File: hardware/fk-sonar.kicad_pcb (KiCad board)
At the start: 2 copper layers, 34.5 x 70.4 mm, 81 parts, among them J1 Conn_01x03, J2 CONN-HDR-2x5, J3 RF-SMA-EDGE, J4 MICRO-USB, J5 S2B-PH-SM4-TB, J6 Conn_01x04, J7 S2B-PH-SM4-TB, J8 Conn_01x03, J9 Conn_01x05, M1 MOUNT_HOLE, M3 MOUNT_HOLE, M4 MOUNT_HOLE, M6 MOUNT_HOLE, Q1 2N7002LT1G, Q2 2N7002LT1G, Q3 2N7002LT1G, Q4 2N7002LT1G, SW1 SPNO, U1 ATSAMD21G18A-AU, U2 RFM95W, U3 BQ24074RGTT, U4 S25FL116K0XMFI041, U5 MAX1704XX, U6 MCP1700T-3302E/MB, Y1 FC-135

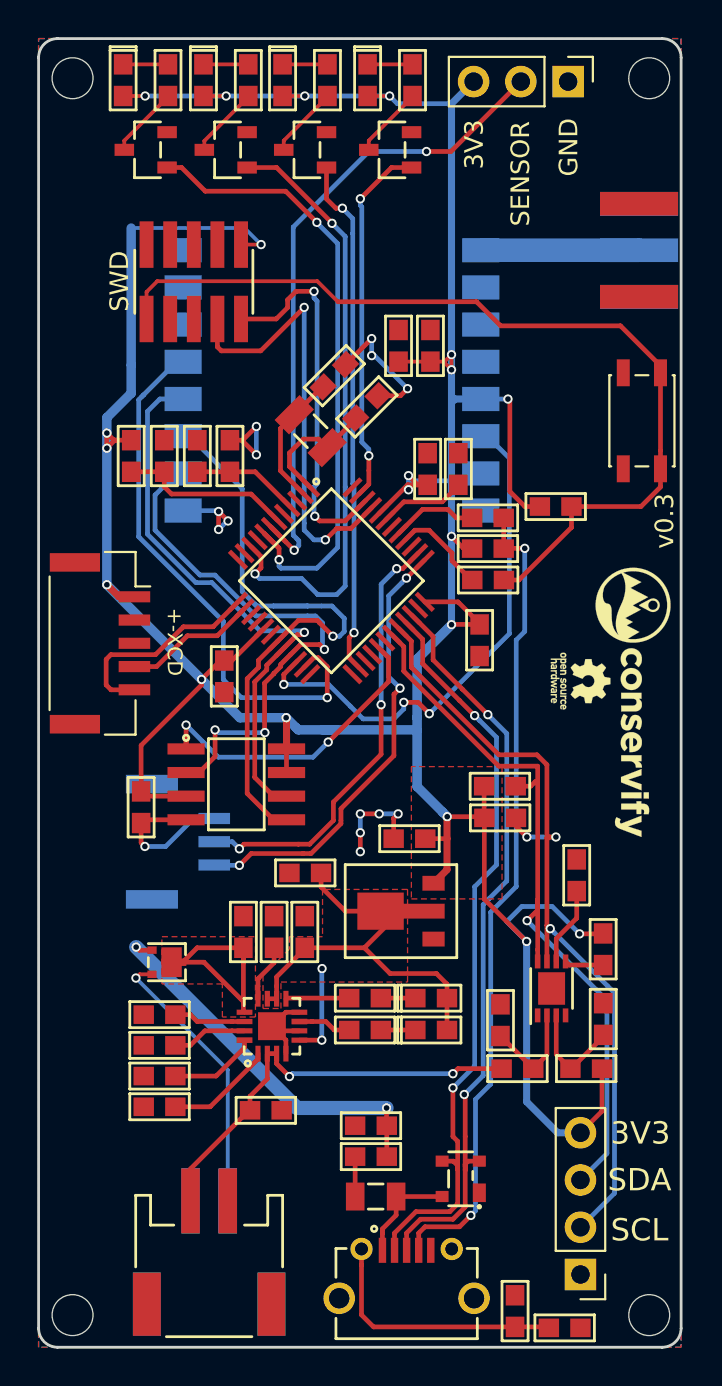
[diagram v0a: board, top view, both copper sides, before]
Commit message: Upgrade to Kicad 5. Also adding SK6812 and molex connectors.
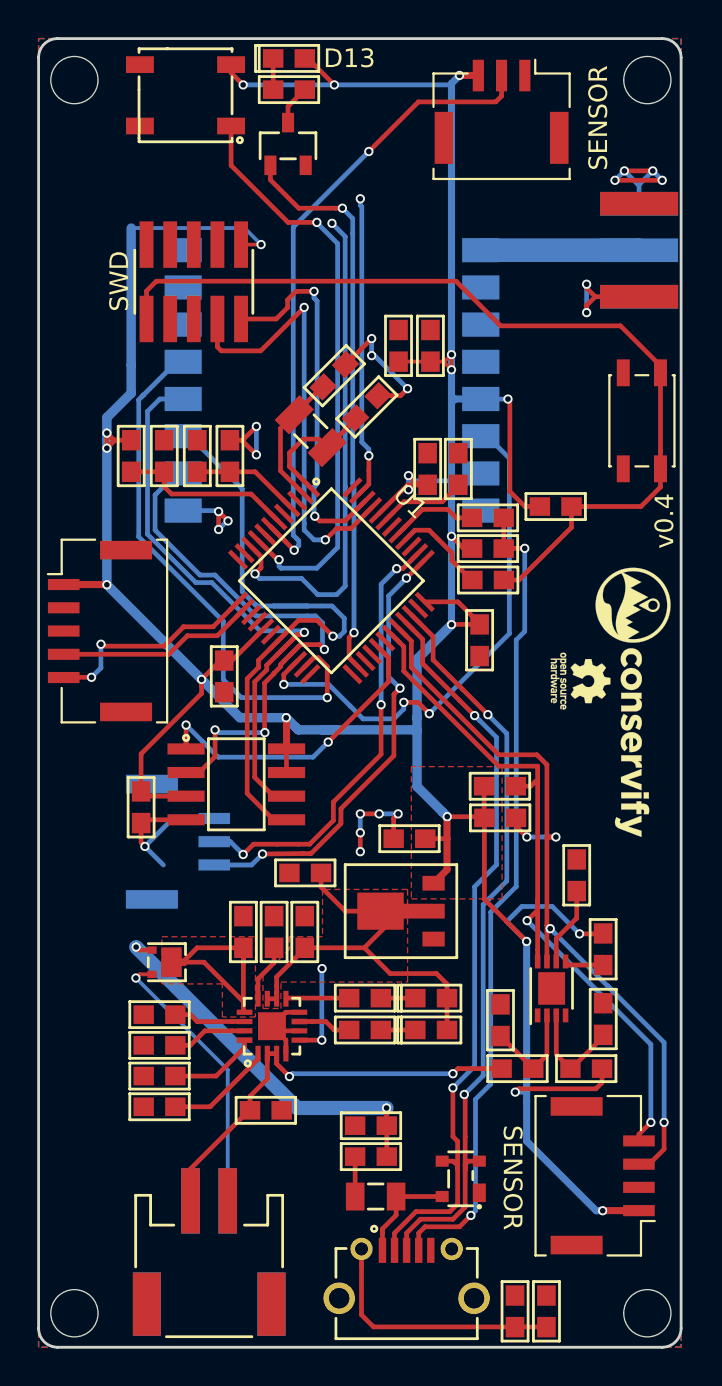
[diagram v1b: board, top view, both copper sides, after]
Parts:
- removed D2: Orange, RocketScreamKicadLibrary:LED-0603
- removed D3: Yellow, RocketScreamKicadLibrary:LED-0603
- removed D4: Blue, RocketScreamKicadLibrary:LED-0603
- removed Q2, Q3, Q4: 2N7002LT1G, RocketScreamKicadLibrary:SOT-23
- removed R4, R5, R6: 2K2, RocketScreamKicadLibrary:RES-0603
- added U7: SK6812, conservify:SK6812, F.Cu at (130.1, 65.3)
- C1, C10, C11, C12, C13, C14, C15, C16, C17, C18, C19, C2, C20, C21, C3, C4, C5, C6, C7, C8, C9: footprint RocketScreamKicadLibrary:CAP-0603 -> conservify:CAP-0603
- D1, D7, D8: footprint RocketScreamKicadLibrary:LED-0603 -> conservify:LED-0603
- D5: footprint RocketScreamKicadLibrary:SOT-1016 -> conservify:SOT-1016
- D6: footprint RocketScreamKicadLibrary:SOT-143B -> conservify:SOT-143B
- F1: footprint RocketScreamKicadLibrary:MF-PSMF020X -> conservify:MF-PSMF020X
- J1: footprint Socket_Strips:Socket_Strip_Straight_1x03_Pitch2.54mm -> conservify:Molex_CLIK-Mate_502382-0370_1x03_P1.25mm_Vertical
- J2: value CONN-HDR-2x5 -> CONN_02x05_SWD; footprint conservify:HDR_2x5_Pitch1.27mm_SMD_JTAG_SWD -> conservify:HDR_02x05_Pitch1.27mm_SMD_SWD
- J3: footprint RocketScreamKicadLibrary:RF-SMA-EDGE -> conservify:RF-SMA-EDGE
- J5, J7: footprint RocketScreamKicadLibrary:S2B-PH-SM4-TB -> conservify:S2B-PH-SM4-TB
- J6: footprint Socket_Strips:Socket_Strip_Straight_1x04_Pitch2.54mm -> conservify:Molex_CLIK-Mate_502382-0470_1x04_P1.25mm_Vertical
- J8: value Conn_01x03 -> CONN_01x03_SERIAL
- J9: footprint conservify:Molex_CLIK-Mate_502386-0570_1x05_P1.25mm_Horizontal -> conservify:Molex_CLIK-Mate_502382-0570_1x05_P1.25mm_Vertical
- L1, L2: footprint RocketScreamKicadLibrary:IND-0603 -> conservify:IND-0603
- M1, M3, M4, M6: footprint RocketScreamKicadLibrary:HOLE_NPTH_2.2MM -> conservify:HOLE_NPTH_2.54MM
- Q1: footprint RocketScreamKicadLibrary:SOT-23 -> conservify:SOT-23
- R1, R10, R11, R12, R13, R14, R15, R16, R17, R18, R19, R2, R20, R21, R22, R3, R7, R8, R9: footprint RocketScreamKicadLibrary:RES-0603 -> conservify:RES-0603
- U1: footprint RocketScreamKicadLibrary:TQFP-48_7x7mm_Pitch0.5mm -> conservify:TQFP-48_7x7mm_Pitch0.5mm
- U2: footprint RocketScreamKicadLibrary:RFM9xW -> conservify:RFM9xW
- U3: footprint RocketScreamKicadLibrary:QFN-16_3x3mm -> conservify:QFN-16_3x3mm
- U4: footprint RocketScreamKicadLibrary:SOIC-8-N -> conservify:SOIC-8-N
- U5: footprint Housings_DFN_QFN:DFN-8-1EP_3x2mm_Pitch0.5mm -> conservify:DFN-8-1EP_3x2mm_Pitch0.5mm
- U6: footprint RocketScreamKicadLibrary:SOT-89 -> conservify:SOT-89
- Y1: footprint RocketScreamKicadLibrary:ABS07 -> conservify:ABS07
- moved D1 8.99 mm to (135.6, 63.3), turned to 0 degrees
- moved Q1 7.66 mm to (135.6, 67.9), turned to 0 degrees
- moved R1 6.52 mm to (135.6, 65.0), turned to 0 degrees
- moved J6 5.44 mm to (152.5, 123.4), turned to 90 degrees
- moved J1 3.93 mm to (147.1, 66.2), turned to 180 degrees
- moved R13 1.32 mm to (149.5, 130.7), turned to 90 degrees
- moved J9 0.66 mm to (125.5, 94.1)
- moved M3 0.14 mm to (124.1, 130.8)
- moved M4 0.14 mm to (154.9, 130.8)
- moved M1 0.14 mm to (154.9, 64.5)
- moved M6 0.14 mm to (124.1, 64.5)
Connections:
- C7 pad 2: GND -> Net-(C7-Pad2)
- J6 pad 1: GND -> 3V3
- J6 pad 2: /SCL1 -> GND
- J6 pad 3: /SDA1 -> /SCL1
- J6 pad 4: 3V3 -> /SDA1
- Q1 pad 1: /A2 -> /D13
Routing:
- net /A2: track 34.7 -> 0.75 mm, vias 2 -> 0
- net /A3: track 0.00 -> 31.5 mm, vias 0 -> 2
- net GND: track 33.3 -> 49.7 mm, vias 14 -> 20
- net /A4: track 32.9 -> 27.1 mm
- net 3V3: track 204.7 -> 209.0 mm, vias 20 -> 21
- net Net-(Q2-Pad3): track 3.88 -> 0.00 mm
- net Net-(Q4-Pad3): track 3.87 -> 0.00 mm
- net Net-(Q3-Pad3): track 3.87 -> 0.00 mm
- net /A5: track 19.7 -> 16.3 mm
- net /SCL3: track 7.77 -> 10.7 mm
- net /D13: track 28.1 -> 30.6 mm
- net Net-(D4-Pad1): track 2.41 -> 0.00 mm
- net Net-(D3-Pad1): track 2.41 -> 0.00 mm
- net Net-(D2-Pad1): track 2.41 -> 0.00 mm
- net Net-(Q1-Pad3): track 3.87 -> 2.14 mm
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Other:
- board text added: "D13"
- board text added: "v0.4"
- board text removed: "+-XCD"
- board text removed: "3V3"
- board text removed: "GND"
- board text removed: "SCL"
- board text removed: "SDA"
- board text removed: "v0.3"

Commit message: Silkscreen cleanup.
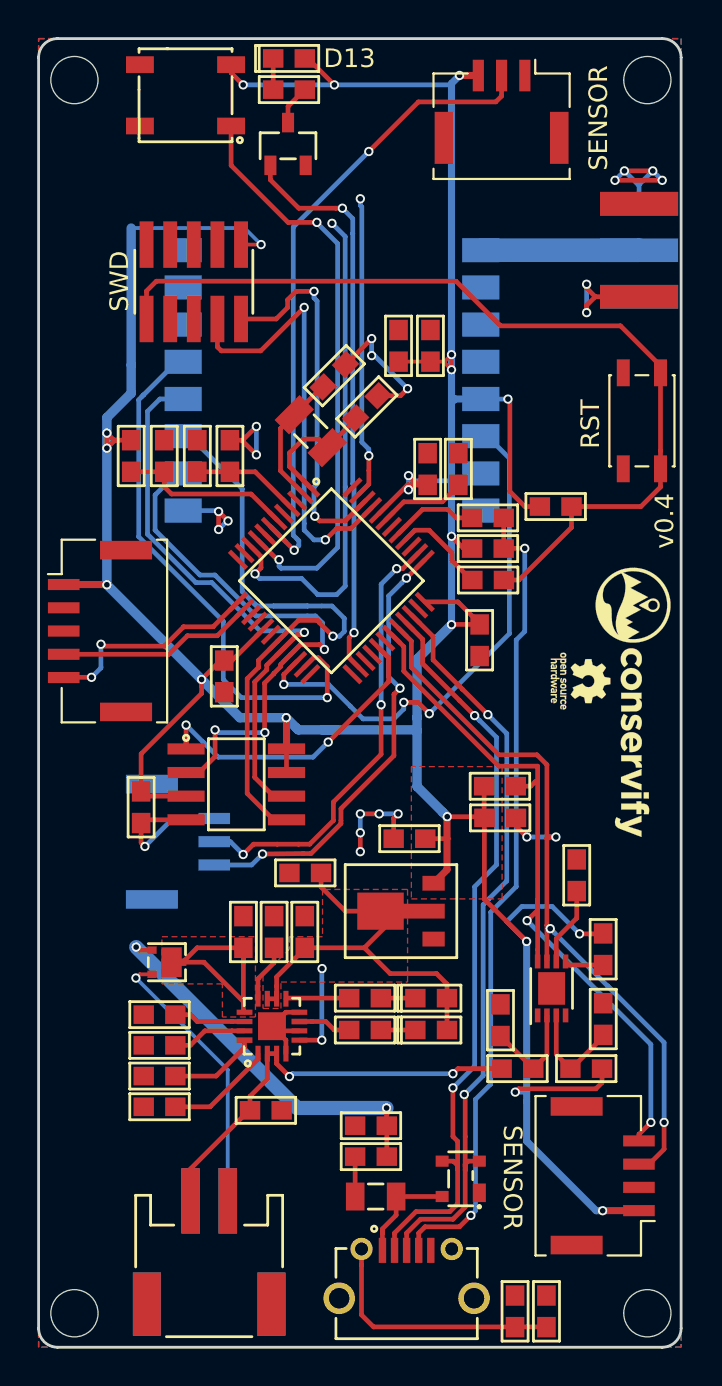
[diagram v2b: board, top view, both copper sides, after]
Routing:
- net GND: track 49.7 -> 48.3 mm
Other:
- board text added: "RST"

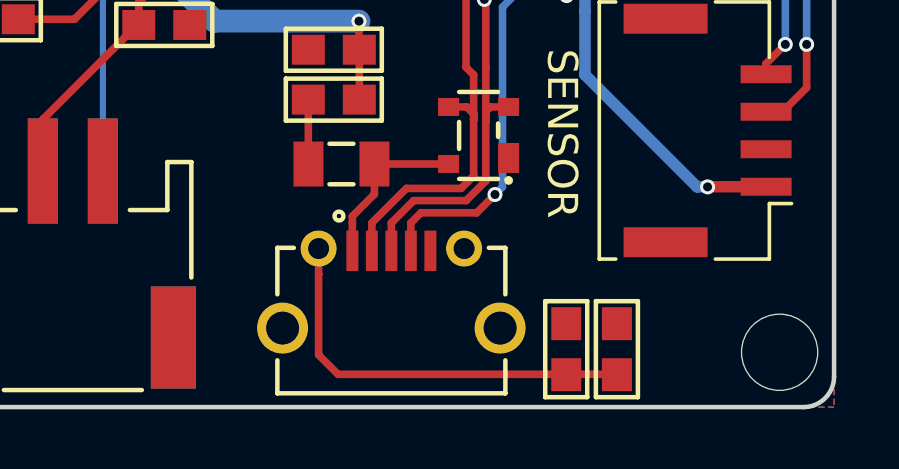
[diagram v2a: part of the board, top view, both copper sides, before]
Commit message: New USB for vertical entry.
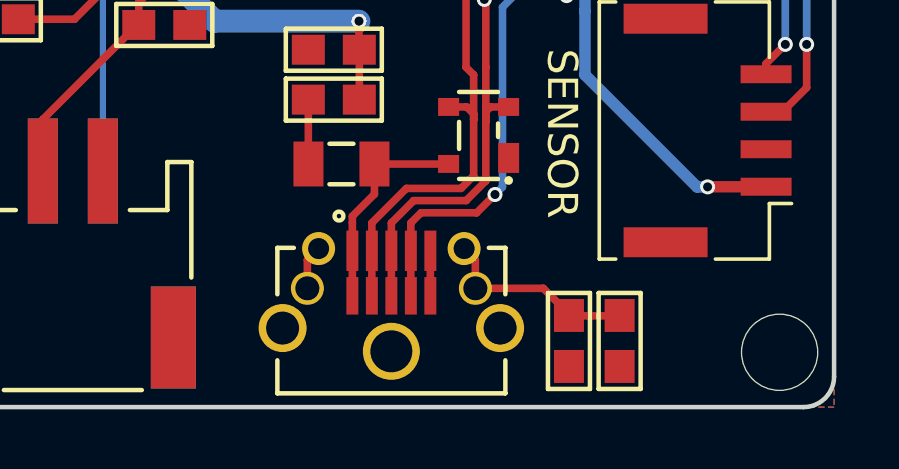
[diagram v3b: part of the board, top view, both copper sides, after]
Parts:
- moved C14 1.80 mm to (149.6, 130.4), turned to 270 degrees
- moved R13 1.62 mm to (147.9, 130.4), turned to 270 degrees
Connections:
- J4 pad 6: Net-(C14-Pad1) -> Net-(J4-Pad6)
- J4 pad 7: Net-(J4-Pad7) -> Net-(C14-Pad1)
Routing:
- net Net-(C14-Pad1): track 13.8 -> 6.78 mm
- net VUSB: track 5.67 -> 7.17 mm
- net GND: track 48.3 -> 49.8 mm
- net /USB-: track 40.5 -> 42.0 mm
- net /USB+: track 40.8 -> 42.3 mm
- net Net-(J4-Pad4): track 44.0 -> 45.5 mm
- net Net-(J4-Pad6): track 0.00 -> 1.48 mm

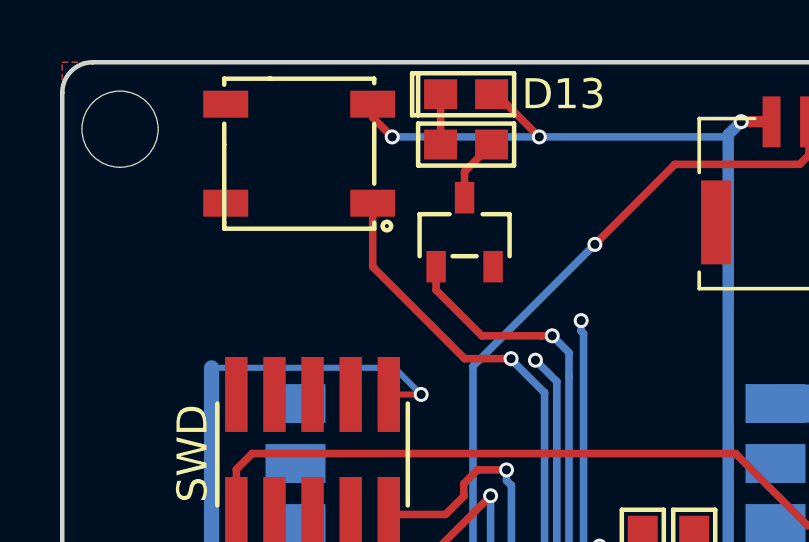
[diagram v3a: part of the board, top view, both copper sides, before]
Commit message: Fix SK6812. Assign easier to read labels to signals.
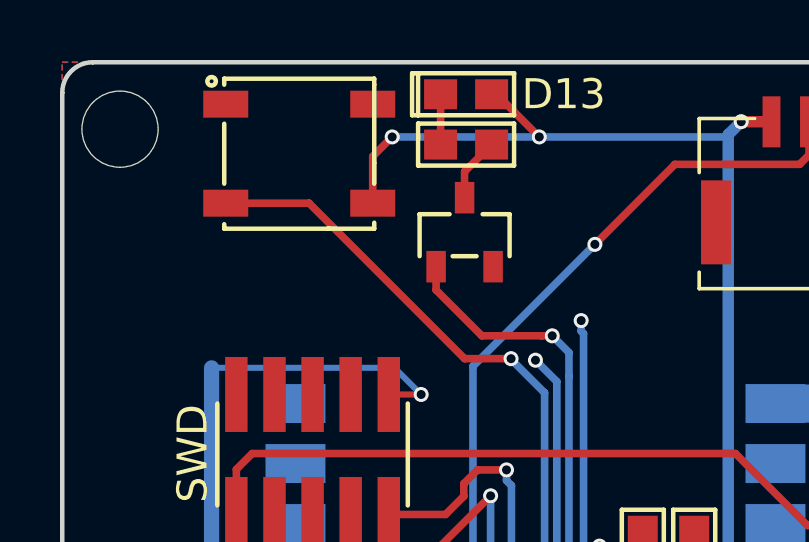
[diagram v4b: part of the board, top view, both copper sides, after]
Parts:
- C1, C10, C15, C16: value 4.7uF 10V X5R -> 4.7uF
- C11: value 1uF 50V X5R -> 1uF
- C12: value 47uF 10V X5R -> 47uF
- C14: value 4.7nF 25V X7R -> 4.7nF
- C17, C19, C21, C6: value 1uF 10V X5R -> 1uF
- J6: value Conn_01x04 -> CONN_01x04
- L1, L2: value BKP1005TS121-T -> BLM18KG221SN1D
- R19: value 1k -> 1K
- turned U7 to 180 degrees
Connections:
- net /FLASH_CS renamed /D6_FLASH_CS
- net /RADIO_CS renamed /D2_RADIO_CS
- net /RADIO_D0 renamed /D38_RADIO_D0
- net Net-(U1-Pad24) renamed /D5
- U7 pad 1: /A3 -> GND
- U7 pad 2: 3V3 -> /A3
- U7 pad 3: Net-(U7-Pad3) -> 3V3
- U7 pad 4: GND -> Net-(U7-Pad4)
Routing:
- net /A3: track 31.5 -> 35.2 mm
- net 3V3: track 209.0 -> 210.1 mm

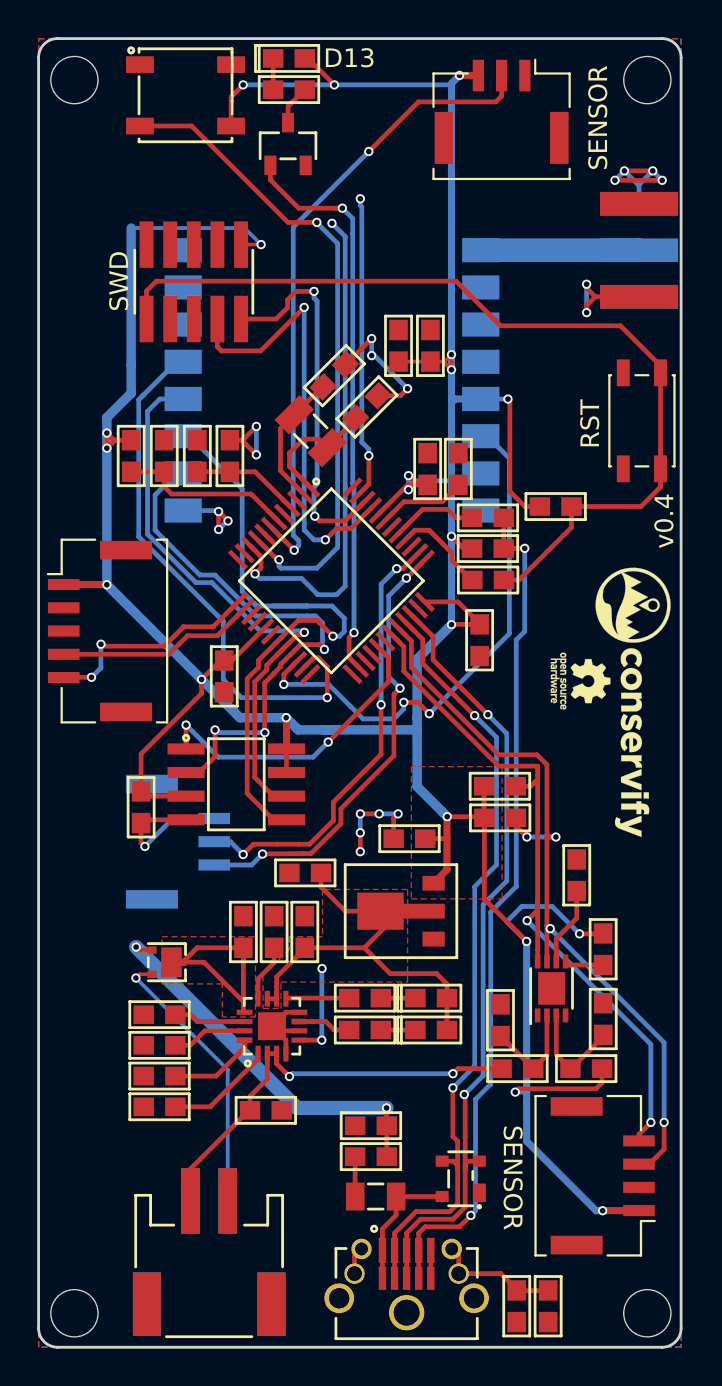
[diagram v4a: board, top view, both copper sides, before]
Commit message: Align connectors on side. Add periph switch.
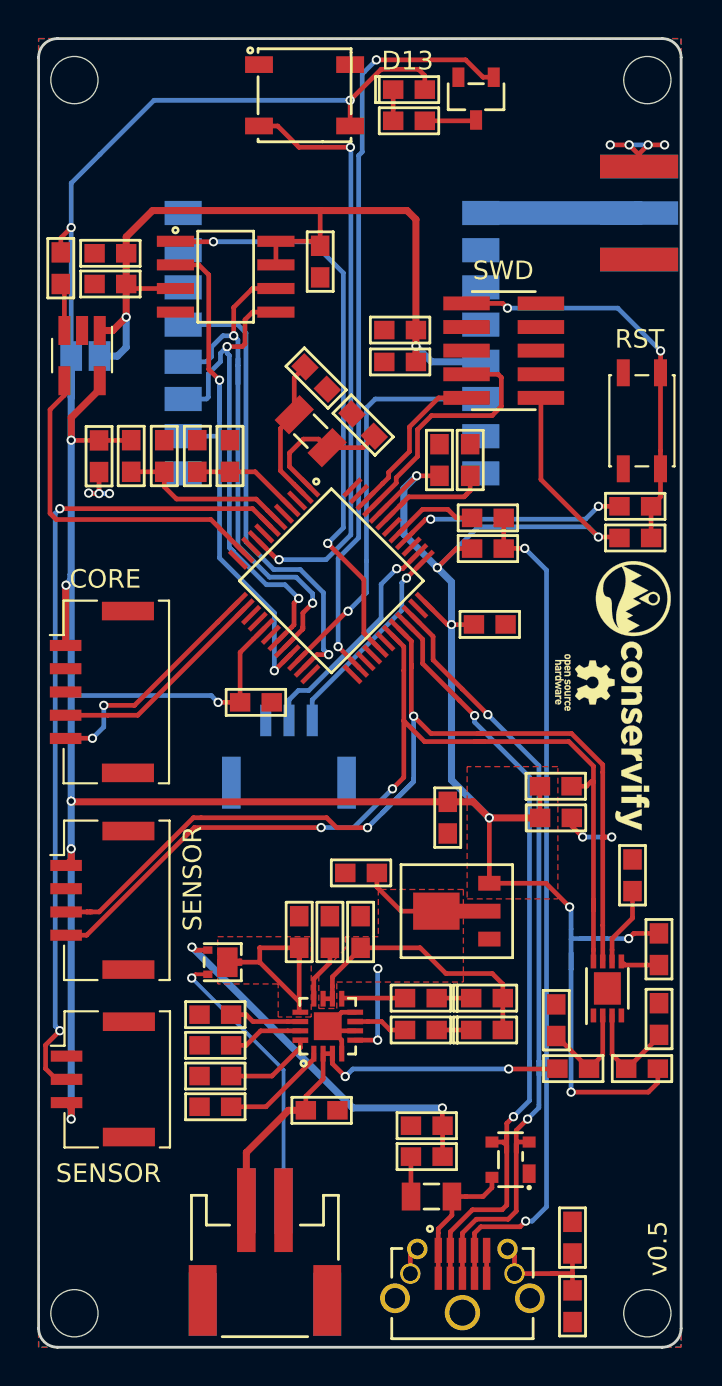
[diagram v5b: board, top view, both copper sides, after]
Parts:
- added C22: 100nF, conservify:CAP-0603, F.Cu at (125.4, 84.7)
- added C23: 100nF, conservify:CAP-0603, F.Cu at (126.0, 75.4)
- added C24: 10uF, conservify:CAP-0603, F.Cu at (126.0, 73.8)
- added J10: CONN_01x02, conservify:SJ_OPEN, B.Cu at (124.7, 79.3)
- added R4: 10K, conservify:RES-0603, F.Cu at (123.4, 74.6)
- added U8: TPS2051B, conservify:SOT-23-5_HandSoldering, F.Cu at (124.5, 79.3)
- J1: value Conn_01x03 -> CONN_01x03
- J9: value Conn_01x05 -> CONN_01x05
- moved J1 56.3 mm to (125.6, 118.2), turned to 270 degrees
- moved C20 30.9 mm to (137.3, 74.2)
- moved J6 30.7 mm to (125.6, 108.6), turned to 270 degrees
- moved U4 27.3 mm to (132.2, 75.0)
- moved J2 17.1 mm to (147.2, 79.0), turned to 90 degrees
- moved Q1 10.4 mm to (145.7, 65.5), turned to 180 degrees
- moved R3 8.85 mm to (154.3, 87.4)
- moved J8 7.52 mm to (135.6, 100.8), turned to 0 degrees
- moved D1 6.67 mm to (142.1, 65.0)
- moved R1 6.67 mm to (142.1, 66.6)
- moved U7 6.40 mm to (136.5, 65.3)
- moved R2 4.60 mm to (154.3, 89.1)
- moved C14 3.91 mm to (150.9, 126.7), turned to 90 degrees
- moved J9 3.28 mm to (125.6, 97.4)
- moved C10 3.00 mm to (143.0, 120.7)
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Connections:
- C12 pad 1: 3V3 -> /PERIPH_3V3
- C13 pad 1: 3V3 -> /PERIPH_3V3
- C20 pad 1: 3V3 -> /PERIPH_3V3
- U1 pad 11: /D8 -> /D8_PERIPH_EN
- U2 pad 13: 3V3 -> /PERIPH_3V3
- U4 pad 3: 3V3 -> /PERIPH_3V3
- U4 pad 7: 3V3 -> /PERIPH_3V3
- U4 pad 8: 3V3 -> /PERIPH_3V3
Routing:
- net /PERIPH_3V3: track 0.00 -> 45.5 mm, vias 0 -> 2
- net GND: track 49.8 -> 13.5 mm, vias 20 -> 7
- net /A4: track 27.1 -> 0.00 mm, vias 2 -> 0
- net /RST: track 48.9 -> 22.1 mm, vias 0 -> 2
- net /D8_PERIPH_EN: track 0.00 -> 18.8 mm
- net /A5: track 16.3 -> 0.00 mm, vias 2 -> 0
- net /SCL1: track 42.6 -> 58.9 mm
- net /D6_FLASH_CS: track 17.2 -> 31.4 mm
- net /SDA1: track 39.5 -> 53.6 mm
- net /D30: track 23.9 -> 11.2 mm, vias 3 -> 1
- net /SWDIO: track 20.3 -> 8.65 mm, vias 2 -> 0
- net /D31: track 23.9 -> 12.4 mm, vias 3 -> 1
- net /SWCLK: track 23.9 -> 13.7 mm, vias 2 -> 0
- net /D13: track 30.6 -> 40.7 mm
- net /A1: track 35.7 -> 43.8 mm
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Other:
- board text added: "CORE"
- board text added: "DEBUG"
- board text added: "v0.5"
- board text removed: "v0.4"

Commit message: Fixing rescued stuff and DRC checks.
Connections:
- net AREF renamed Net-(C1-Pad1)
- C7 pad 2: Net-(C7-Pad2) -> GND
